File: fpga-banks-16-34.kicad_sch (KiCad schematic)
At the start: 25 parts, among them U1 ASFLMB-100.000MHZ-XY-T, U15 XC7K160T-FFG676, U8 PCA9517ADMR2G

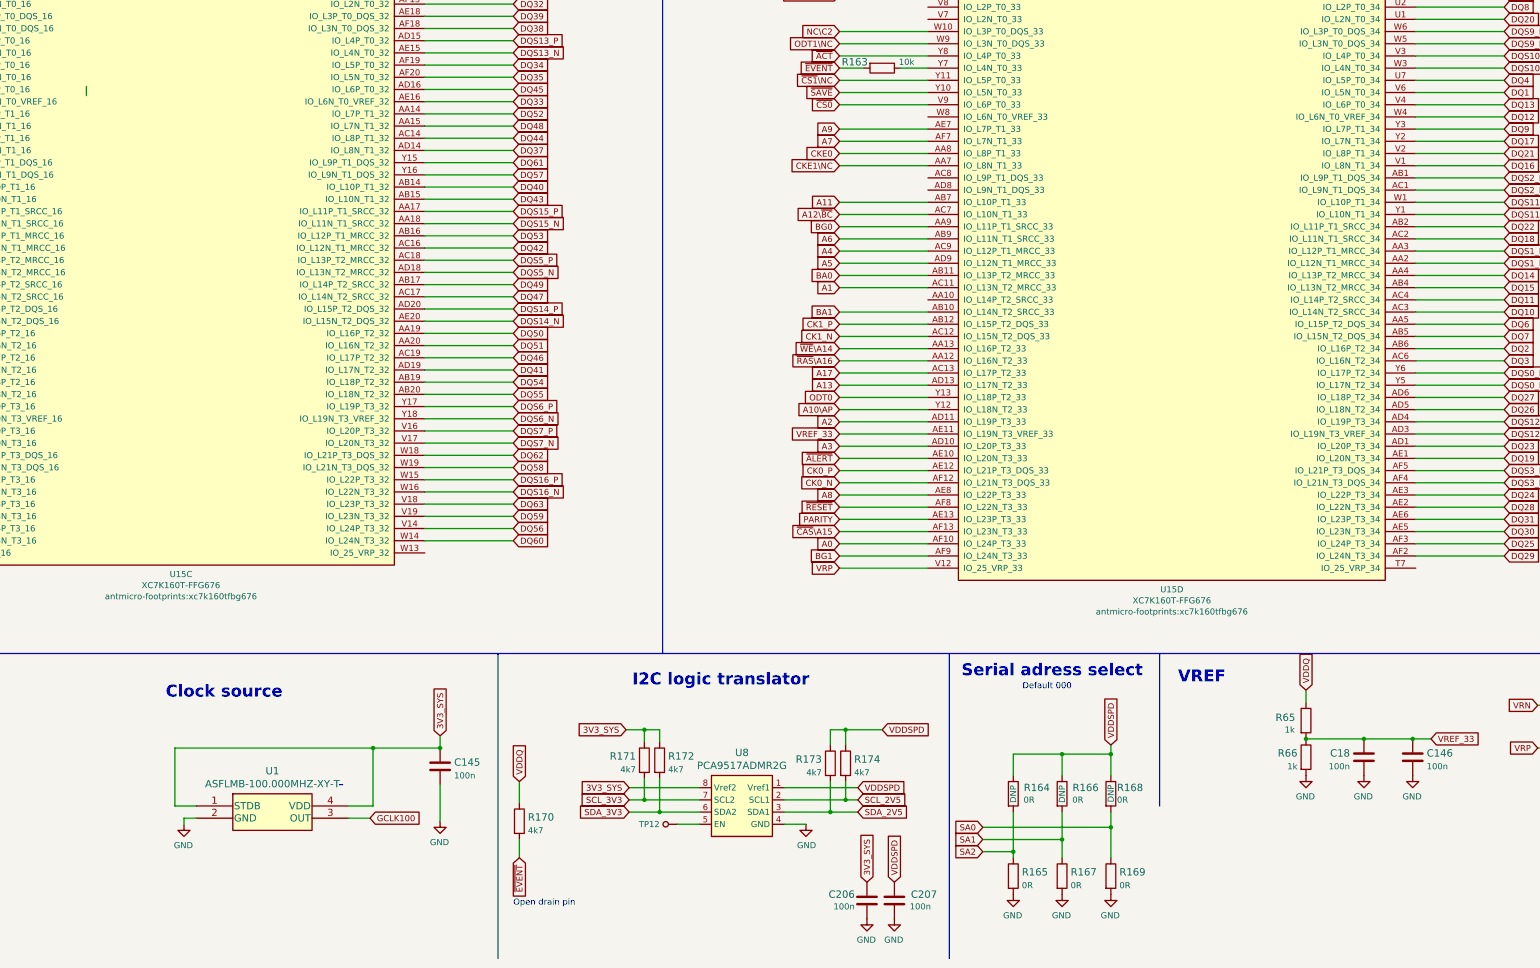
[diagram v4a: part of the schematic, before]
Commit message: Implement all review fixes, route control signals from FMC to FPGA
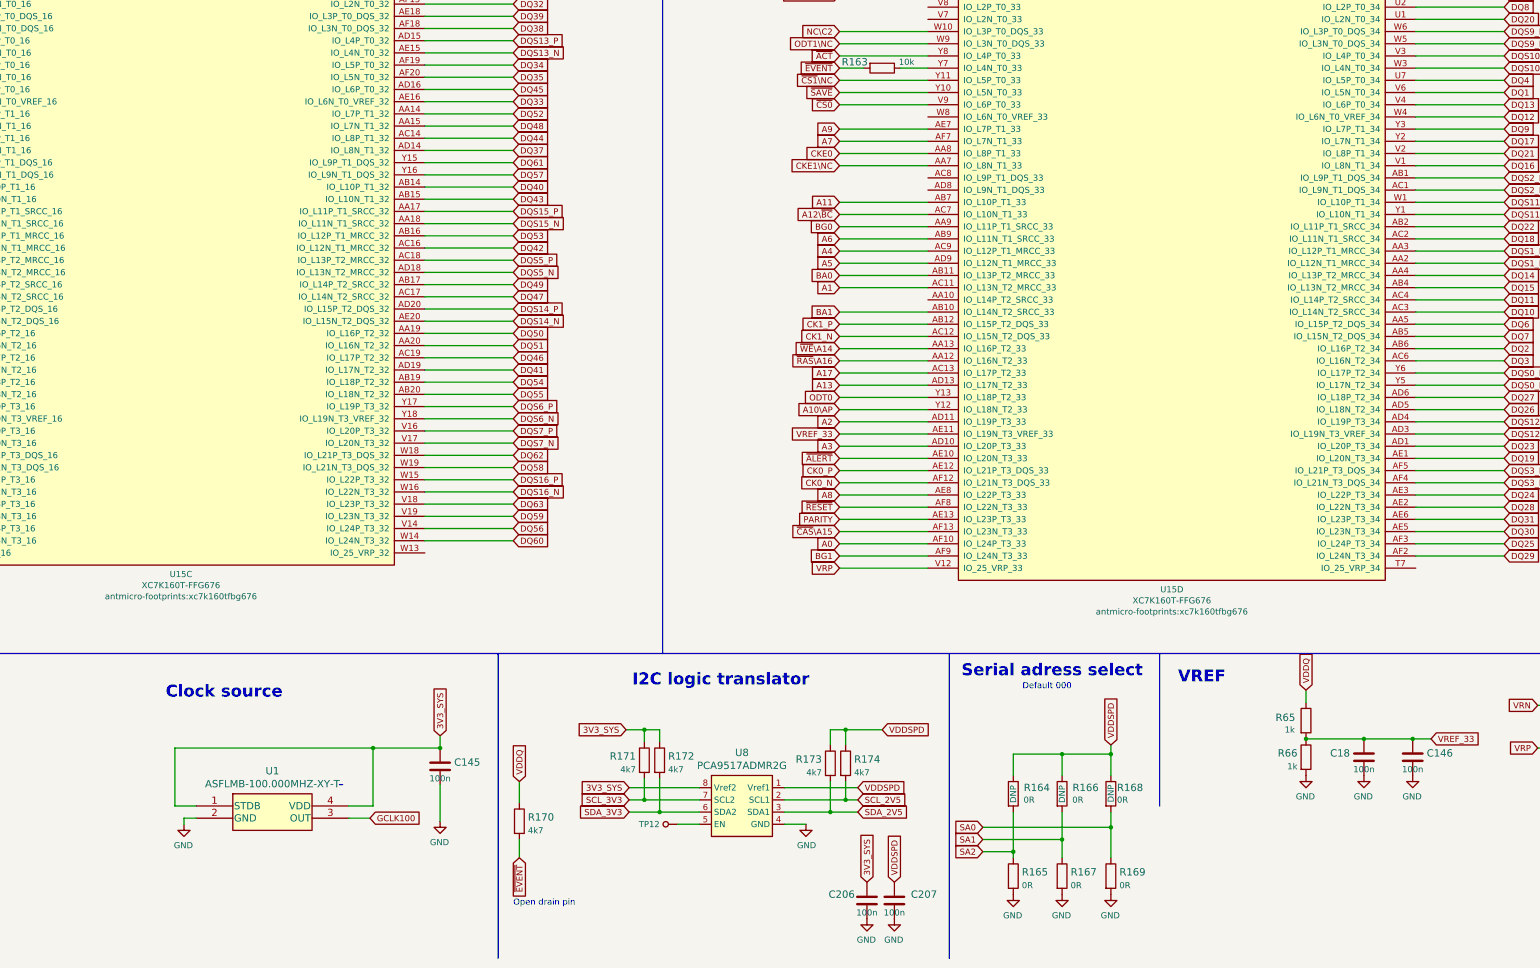
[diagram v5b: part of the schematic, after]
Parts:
- C145, C146, C18, C206, C207: value C_100n_0402_6V3 -> C_100n_0402; footprint data-center-dram-tester-footprints:0402-cap -> antmicro-footprints:0402-cap; symbol data-center-dram-tester:C_100n_0402_6V3 -> antmicroCapacitors0402:C_100n_0402; MPN 0402X104K6R3CT -> GRM155R61H104KE14D; Manufacturer Walsin -> Murata
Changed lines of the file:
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@@
     (stroke (width 0) (type default) (color 0 0 0 0))
   )
-  (wire (pts (xy 76.835 105.41) (xy 76.835 103.505))
-    (stroke (width 0) (type default) (color 0 0 0 0))
-  )
   (wire (pts (xy 58.42 55.88) (xy 58.42 50.165))
     (stroke (width 0) (type default) (color 0 0 0 0))
@@
     (pin "1")
   )
-  (symbol (lib_id "data-center-dram-tester:C_100n_0402_6V3") (at 353.06 243.205 0) (mirror y) (unit 1)
+  (symbol (lib_id "antmicroCapacitors0402:C_100n_0402") (at 353.06 243.205 0) (mirror y) (unit 1)
     (in_bom yes) (on_board yes) (fields_autoplaced)
     (property "Reference" "C146" (id 0) (at 355.981 242.3704 0)
       (effects (font (size 1.524 1.524)) (justify right))
     )
-    (property "Value" "C_100n_0402_6V3" (id 1) (at 353.06 247.015 0)
+    (property "Value" "C_100n_0402" (id 1) (at 353.06 247.015 0)
       (effects (font (size 1.524 1.524)) hide)
     )
-    (property "Footprint" "data-center-dram-tester-footprints:0402-cap" (id 2) (at 347.98 238.125 0)
+    (property "Footprint" "antmicro-footprints:0402-cap" (id 2) (at 347.98 238.125 0)
       (effects (font (size 1.524 1.524)) (justify left) hide)
     )
@@
       (effects (font (size 1.27 1.27)) hide)
     )
-    (property "Manufacturer" "Walsin" (id 4) (at 347.98 233.045 0)
+    (property "Manufacturer" "Murata" (id 4) (at 347.98 233.045 0)
       (effects (font (size 1.524 1.524)) (justify left) hide)
     )
-    (property "MPN" "0402X104K6R3CT" (id 5) (at 347.98 235.585 0)
+    (property "MPN" "GRM155R61H104KE14D" (id 5) (at 347.98 235.585 0)
       (effects (font (size 1.524 1.524)) (justify left) hide)
     )
-    (property "Val" "100n" (id 6) (at 355.981 245.1355 0)
-      (effects (font (size 1.27 1.27)) (justify right))
-    )
+    (property "Val" "100n" (id 6) (at 353.06 245.745 0))
     (pin "1")
     (pin "2")
   )
-  (symbol (lib_id "data-center-dram-tester:C_100n_0402_6V3") (at 342.9 243.205 0) (mirror y) (unit 1)
+  (symbol (lib_id "antmicroCapacitors0402:C_100n_0402") (at 342.9 243.205 0) (mirror y) (unit 1)
     (in_bom yes) (on_board yes) (fields_autoplaced)
     (property "Reference" "C18" (id 0) (at 339.979 242.3704 0)
       (effects (font (size 1.524 1.524)) (justify left))
     )
-    (property "Value" "C_100n_0402_6V3" (id 1) (at 342.9 247.015 0)
+    (property "Value" "C_100n_0402" (id 1) (at 342.9 247.015 0)
       (effects (font (size 1.524 1.524)) hide)
     )
-    (property "Footprint" "data-center-dram-tester-footprints:0402-cap" (id 2) (at 337.82 238.125 0)
+    (property "Footprint" "antmicro-footprints:0402-cap" (id 2) (at 337.82 238.125 0)
       (effects (font (size 1.524 1.524)) (justify left) hide)
     )
@@
       (effects (font (size 1.27 1.27)) hide)
     )
-    (property "Manufacturer" "Walsin" (id 4) (at 337.82 233.045 0)
+    (property "Manufacturer" "Murata" (id 4) (at 337.82 233.045 0)
       (effects (font (size 1.524 1.524)) (justify left) hide)
     )
-    (property "MPN" "0402X104K6R3CT" (id 5) (at 337.82 235.585 0)
+    (property "MPN" "GRM155R61H104KE14D" (id 5) (at 337.82 235.585 0)
       (effects (font (size 1.524 1.524)) (justify left) hide)
     )
-    (property "Val" "100n" (id 6) (at 339.979 245.1355 0)
-      (effects (font (size 1.27 1.27)) (justify left))
-    )
+    (property "Val" "100n" (id 6) (at 342.9 245.745 0))
     (pin "1")
     (pin "2")
@@
     (pin "1")
   )
-  (symbol (lib_id "data-center-dram-tester:C_100n_0402_6V3") (at 239.395 273.05 0) (mirror y) (unit 1)
+  (symbol (lib_id "antmicroCapacitors0402:C_100n_0402") (at 239.395 273.05 0) (mirror y) (unit 1)
     (in_bom yes) (on_board yes)
     (property "Reference" "C206" (id 0) (at 236.855 271.78 0)
       (effects (font (size 1.524 1.524)) (justify left))
     )
-    (property "Value" "C_100n_0402_6V3" (id 1) (at 239.395 276.86 0)
+    (property "Value" "C_100n_0402" (id 1) (at 239.395 276.86 0)
       (effects (font (size 1.524 1.524)) hide)
     )
-    (property "Footprint" "data-center-dram-tester-footprints:0402-cap" (id 2) (at 234.315 267.97 0)
+    (property "Footprint" "antmicro-footprints:0402-cap" (id 2) (at 234.315 267.97 0)
       (effects (font (size 1.524 1.524)) (justify left) hide)
     )
@@
       (effects (font (size 1.27 1.27)) hide)
     )
-    (property "Manufacturer" "Walsin" (id 4) (at 234.315 262.89 0)
+    (property "Manufacturer" "Murata" (id 4) (at 234.315 262.89 0)
       (effects (font (size 1.524 1.524)) (justify left) hide)
     )
-    (property "MPN" "0402X104K6R3CT" (id 5) (at 234.315 265.43 0)
+    (property "MPN" "GRM155R61H104KE14D" (id 5) (at 234.315 265.43 0)
       (effects (font (size 1.524 1.524)) (justify left) hide)
     )
-    (property "Val" "100n" (id 6) (at 236.855 274.32 0)
-      (effects (font (size 1.27 1.27)) (justify left))
-    )
+    (property "Val" "100n" (id 6) (at 239.395 275.59 0))
     (pin "1")
     (pin "2")
@@
     (pin "1")
   )
-  (symbol (lib_id "data-center-dram-tester:C_100n_0402_6V3") (at 245.11 273.05 0) (mirror y) (unit 1)
+  (symbol (lib_id "antmicroCapacitors0402:C_100n_0402") (at 245.11 273.05 0) (mirror y) (unit 1)
     (in_bom yes) (on_board yes)
     (property "Reference" "C207" (id 0) (at 254 271.78 0)
       (effects (font (size 1.524 1.524)) (justify left))
     )
-    (property "Value" "C_100n_0402_6V3" (id 1) (at 245.11 276.86 0)
+    (property "Value" "C_100n_0402" (id 1) (at 245.11 276.86 0)
       (effects (font (size 1.524 1.524)) hide)
     )
-    (property "Footprint" "data-center-dram-tester-footprints:0402-cap" (id 2) (at 240.03 267.97 0)
+    (property "Footprint" "antmicro-footprints:0402-cap" (id 2) (at 240.03 267.97 0)
       (effects (font (size 1.524 1.524)) (justify left) hide)
     )
@@
       (effects (font (size 1.27 1.27)) hide)
     )
-    (property "Manufacturer" "Walsin" (id 4) (at 240.03 262.89 0)
+    (property "Manufacturer" "Murata" (id 4) (at 240.03 262.89 0)
       (effects (font (size 1.524 1.524)) (justify left) hide)
     )
-    (property "MPN" "0402X104K6R3CT" (id 5) (at 240.03 265.43 0)
+    (property "MPN" "GRM155R61H104KE14D" (id 5) (at 240.03 265.43 0)
       (effects (font (size 1.524 1.524)) (justify left) hide)
     )
-    (property "Val" "100n" (id 6) (at 252.73 274.32 0)
-      (effects (font (size 1.27 1.27)) (justify left))
-    )
+    (property "Val" "100n" (id 6) (at 245.11 275.59 0))
     (pin "1")
     (pin "2")
@@
     (pin "1")
   )
-  (symbol (lib_id "data-center-dram-tester:C_100n_0402_6V3") (at 150.495 245.11 0) (mirror y) (unit 1)
+  (symbol (lib_id "antmicroCapacitors0402:C_100n_0402") (at 150.495 245.11 0) (mirror y) (unit 1)
     (in_bom yes) (on_board yes) (fields_autoplaced)
     (property "Reference" "C145" (id 0) (at 153.416 244.2754 0)
       (effects (font (size 1.524 1.524)) (justify right))
     )
-    (property "Value" "C_100n_0402_6V3" (id 1) (at 150.495 248.92 0)
+    (property "Value" "C_100n_0402" (id 1) (at 150.495 248.92 0)
       (effects (font (size 1.524 1.524)) hide)
     )
-    (property "Footprint" "data-center-dram-tester-footprints:0402-cap" (id 2) (at 145.415 240.03 0)
+    (property "Footprint" "antmicro-footprints:0402-cap" (id 2) (at 145.415 240.03 0)
       (effects (font (size 1.524 1.524)) (justify left) hide)
     )
@@
       (effects (font (size 1.27 1.27)) hide)
     )
-    (property "Manufacturer" "Walsin" (id 4) (at 145.415 234.95 0)
+    (property "Manufacturer" "Murata" (id 4) (at 145.415 234.95 0)
       (effects (font (size 1.524 1.524)) (justify left) hide)
     )
-    (property "MPN" "0402X104K6R3CT" (id 5) (at 145.415 237.49 0)
+    (property "MPN" "GRM155R61H104KE14D" (id 5) (at 145.415 237.49 0)
       (effects (font (size 1.524 1.524)) (justify left) hide)
     )
-    (property "Val" "100n" (id 6) (at 153.416 247.0405 0)
-      (effects (font (size 1.27 1.27)) (justify right))
-    )
+    (property "Val" "100n" (id 6) (at 150.495 247.65 0))
     (pin "1")
     (pin "2")
